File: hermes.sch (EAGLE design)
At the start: 36 parts, among them IC1 MIC5219-3.3BML

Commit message: -Update Library -Correct P2P pins -Place general position of components
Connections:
- net +3V3: now also IC1G$1.OUT; no longer IC1.OUT
- net GND: now also CONN2-3.P$1, IC1-DICE.P$1, IC1G$1.GND; no longer CONN2-2.P$1, IC1.GND
- net N$2: now also IC1G$1.PG; no longer IC1.PG
- net SERCOM5_SCL: now also CONN2-1.P$1; no longer CONN2-4.P$1
- net SERCOM5_SDA: now also CONN2-2.P$1; no longer CONN2-3.P$1
- net VCC: now also CONN2-4.P$1, IC1G$1.EN, IC1G$1.IN; no longer CONN2-1.P$1, IC1.EN, IC1.IN
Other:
- moved on the sheet: CONN2-1, CONN2-2, CONN2-3, CONN2-4
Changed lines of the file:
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@@
 <instance part="CONN1" gate="-3" x="119.38" y="40.64" rot="MR0"/>
 <instance part="CONN1" gate="-4" x="119.38" y="35.56" rot="MR0"/>
-<instance part="CONN2" gate="-1" x="127" y="60.96"/>
-<instance part="CONN2" gate="-2" x="127" y="55.88"/>
-<instance part="CONN2" gate="-3" x="127" y="40.64"/>
-<instance part="CONN2" gate="-4" x="127" y="35.56"/>
+<instance part="CONN2" gate="-1" x="127" y="35.56" rot="MR180"/>
+<instance part="CONN2" gate="-3" x="127" y="55.88"/>
+<instance part="CONN2" gate="-2" x="127" y="40.64"/>
+<instance part="CONN2" gate="-4" x="127" y="60.96"/>
 <instance part="U$1" gate="-1" x="20.32" y="60.96" rot="MR0"/>
 <instance part="U$1" gate="-2" x="20.32" y="55.88" rot="MR0"/>
@@
 <instance part="U$1" gate="-DICE" x="185.42" y="50.8" rot="R180"/>
 <instance part="GND14" gate="1" x="187.96" y="45.72"/>
+<instance part="IC1" gate="-DICE" x="185.42" y="66.04" rot="R180"/>
 </instances>
 <busses>
@@
 <junction x="124.46" y="55.88"/>
 <pinref part="CONN1" gate="-2" pin="P$1"/>
-<pinref part="CONN2" gate="-2" pin="P$1"/>
+<pinref part="CONN2" gate="-3" pin="P$1"/>
 </segment>
 <segment>
@@
 <wire x1="185.42" y1="50.8" x2="187.96" y2="50.8" width="0.1524" layer="91"/>
 <junction x="187.96" y="50.8"/>
+<pinref part="IC1" gate="-DICE" pin="P$1"/>
+<wire x1="185.42" y1="66.04" x2="187.96" y2="66.04" width="0.1524" layer="91"/>
+<wire x1="187.96" y1="66.04" x2="187.96" y2="60.96" width="0.1524" layer="91"/>
+<junction x="187.96" y="60.96"/>
 </segment>
 </net>
@@
 <wire x1="119.38" y1="60.96" x2="124.46" y2="60.96" width="0.1524" layer="91"/>
 <pinref part="P+3" gate="VCC" pin="VCC"/>
-<wire x1="124.46" y1="60.96" x2="127" y2="60.96" width="0.1524" layer="91"/>
 <wire x1="124.46" y1="63.5" x2="124.46" y2="60.96" width="0.1524" layer="91"/>
+<pinref part="CONN1" gate="-1" pin="P$1"/>
+<pinref part="CONN2" gate="-4" pin="P$1"/>
+<wire x1="127" y1="60.96" x2="124.46" y2="60.96" width="0.1524" layer="91"/>
 <junction x="124.46" y="60.96"/>
-<pinref part="CONN1" gate="-1" pin="P$1"/>
-<pinref part="CONN2" gate="-1" pin="P$1"/>
 </segment>
 </net>
@@
 <label x="127" y="33.02" size="1.27" layer="95" xref="yes"/>
 <pinref part="CONN1" gate="-3" pin="P$1"/>
-<pinref part="CONN2" gate="-3" pin="P$1"/>
+<pinref part="CONN2" gate="-2" pin="P$1"/>
 </segment>
 </net>
@@
 <net name="SERCOM5_SCL" class="0">
 <segment>
-<wire x1="127" y1="35.56" x2="121.92" y2="35.56" width="0.1524" layer="91"/>
 <wire x1="121.92" y1="35.56" x2="119.38" y2="35.56" width="0.1524" layer="91"/>
 <wire x1="121.92" y1="35.56" x2="121.92" y2="30.48" width="0.1524" layer="91"/>
-<junction x="121.92" y="35.56"/>
 <wire x1="121.92" y1="30.48" x2="127" y2="30.48" width="0.1524" layer="91"/>
 <label x="127" y="30.48" size="1.27" layer="95" xref="yes"/>
 <pinref part="CONN1" gate="-4" pin="P$1"/>
-<pinref part="CONN2" gate="-4" pin="P$1"/>
-</segment>
-</net>
+<pinref part="CONN2" gate="-1" pin="P$1"/>
+<wire x1="127" y1="35.56" x2="121.92" y2="35.56" width="0.1524" layer="91"/>
+<junction x="121.92" y="35.56"/>
+</segment>
+</net>

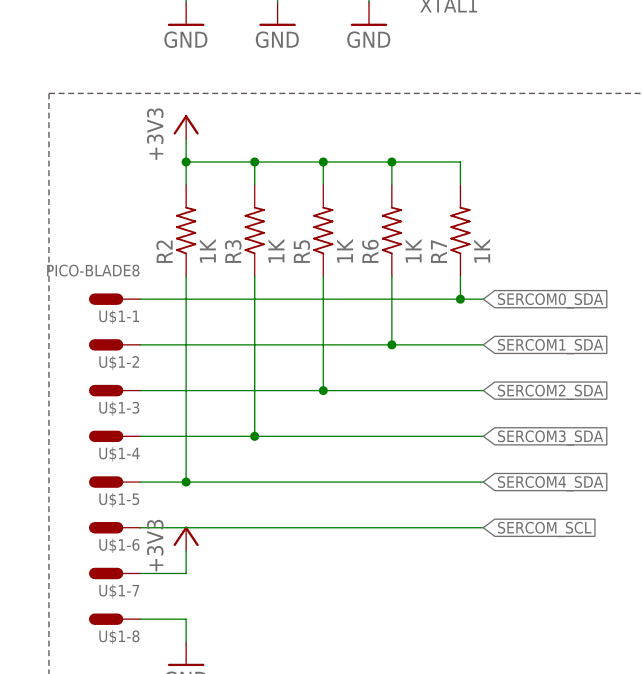
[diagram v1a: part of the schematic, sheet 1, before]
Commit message: MIniaturization of board process
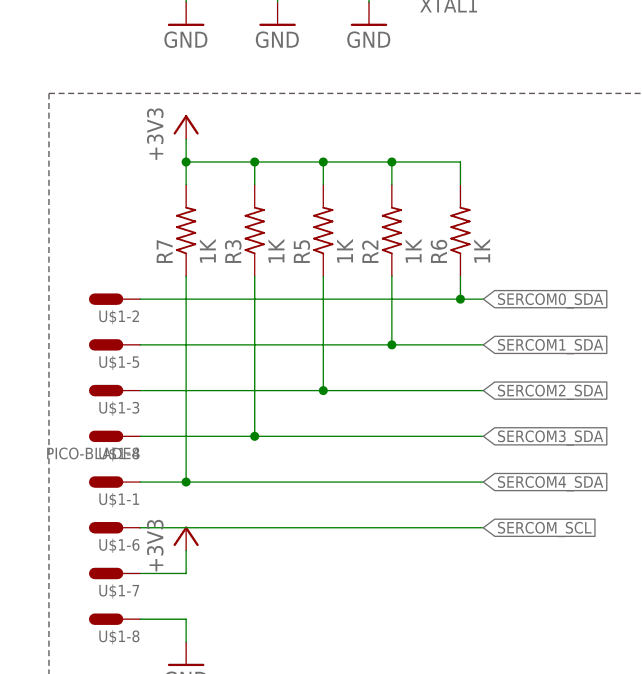
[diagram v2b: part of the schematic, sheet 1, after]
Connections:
- net SERCOM0_SDA: now also R6.1, U$1-2.P$1; no longer R7.1, U$1-1.P$1
- net SERCOM1_SDA: now also R2.1, U$1-5.P$1; no longer R6.1, U$1-2.P$1
- net SERCOM4_SDA: now also R7.1, U$1-1.P$1; no longer R2.1, U$1-5.P$1
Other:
- moved on the sheet: R2, R6, R7, U$1-1, U$1-2, U$1-5
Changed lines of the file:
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@@
 <instance part="GND5" gate="1" x="45.72" y="104.14"/>
 <instance part="+3V31" gate="G$1" x="25.4" y="81.28"/>
-<instance part="R7" gate="G$1" x="55.88" y="68.58" rot="R90"/>
-<instance part="R6" gate="G$1" x="48.26" y="68.58" rot="R90"/>
+<instance part="R7" gate="G$1" x="25.4" y="68.58" rot="R90"/>
+<instance part="R6" gate="G$1" x="55.88" y="68.58" rot="R90"/>
 <instance part="R5" gate="G$1" x="40.64" y="68.58" rot="R90"/>
 <instance part="R3" gate="G$1" x="33.02" y="68.58" rot="R90"/>
-<instance part="R2" gate="G$1" x="25.4" y="68.58" rot="R90"/>
+<instance part="R2" gate="G$1" x="48.26" y="68.58" rot="R90"/>
 <instance part="FRAME1" gate="G$1" x="0" y="0"/>
 <instance part="C1" gate="G$1" x="50.8" y="139.7"/>
@@
 <instance part="CONN2" gate="-2" x="127" y="40.64"/>
 <instance part="CONN2" gate="-4" x="127" y="60.96"/>
-<instance part="U$1" gate="-1" x="20.32" y="60.96" rot="MR0"/>
-<instance part="U$1" gate="-2" x="20.32" y="55.88" rot="MR0"/>
+<instance part="U$1" gate="-1" x="20.32" y="40.64" rot="MR0"/>
+<instance part="U$1" gate="-5" x="20.32" y="55.88" rot="MR0"/>
 <instance part="U$1" gate="-3" x="20.32" y="50.8" rot="MR0"/>
 <instance part="U$1" gate="-4" x="20.32" y="45.72" rot="MR0"/>
-<instance part="U$1" gate="-5" x="20.32" y="40.64" rot="MR0"/>
+<instance part="U$1" gate="-2" x="20.32" y="60.96" rot="MR0"/>
 <instance part="U$1" gate="-6" x="20.32" y="35.56" rot="MR0"/>
 <instance part="U$1" gate="-7" x="20.32" y="30.48" rot="MR0"/>
@@
 </segment>
 <segment>
-<pinref part="R2" gate="G$1" pin="2"/>
 <wire x1="55.88" y1="76.2" x2="48.26" y2="76.2" width="0.1524" layer="91"/>
 <wire x1="48.26" y1="76.2" x2="40.64" y2="76.2" width="0.1524" layer="91"/>
 <wire x1="40.64" y1="76.2" x2="33.02" y2="76.2" width="0.1524" layer="91"/>
 <wire x1="33.02" y1="76.2" x2="25.4" y2="76.2" width="0.1524" layer="91"/>
-<wire x1="25.4" y1="76.2" x2="25.4" y2="73.66" width="0.1524" layer="91"/>
 <pinref part="R3" gate="G$1" pin="2"/>
 <wire x1="33.02" y1="73.66" x2="33.02" y2="76.2" width="0.1524" layer="91"/>
@@
 <wire x1="40.64" y1="73.66" x2="40.64" y2="76.2" width="0.1524" layer="91"/>
 <junction x="40.64" y="76.2"/>
-<pinref part="R6" gate="G$1" pin="2"/>
+<pinref part="+3V31" gate="G$1" pin="+3V3"/>
+<wire x1="25.4" y1="78.74" x2="25.4" y2="76.2" width="0.1524" layer="91"/>
+<pinref part="R7" gate="G$1" pin="2"/>
+<wire x1="25.4" y1="73.66" x2="25.4" y2="76.2" width="0.1524" layer="91"/>
+<junction x="25.4" y="76.2"/>
+<pinref part="R2" gate="G$1" pin="2"/>
 <wire x1="48.26" y1="73.66" x2="48.26" y2="76.2" width="0.1524" layer="91"/>
 <junction x="48.26" y="76.2"/>
-<pinref part="R7" gate="G$1" pin="2"/>
+<pinref part="R6" gate="G$1" pin="2"/>
 <wire x1="55.88" y1="73.66" x2="55.88" y2="76.2" width="0.1524" layer="91"/>
-<pinref part="+3V31" gate="G$1" pin="+3V3"/>
-<wire x1="25.4" y1="78.74" x2="25.4" y2="76.2" width="0.1524" layer="91"/>
-<junction x="25.4" y="76.2"/>
 </segment>
 <segment>
@@
 <net name="SERCOM0_SDA" class="0">
 <segment>
-<pinref part="R7" gate="G$1" pin="1"/>
+<label x="58.42" y="60.96" size="1.27" layer="95" xref="yes"/>
+<pinref part="R6" gate="G$1" pin="1"/>
+<wire x1="55.88" y1="60.96" x2="58.42" y2="60.96" width="0.1524" layer="91"/>
 <wire x1="55.88" y1="63.5" x2="55.88" y2="60.96" width="0.1524" layer="91"/>
-<wire x1="55.88" y1="60.96" x2="58.42" y2="60.96" width="0.1524" layer="91"/>
-<label x="58.42" y="60.96" size="1.27" layer="95" xref="yes"/>
+<pinref part="U$1" gate="-2" pin="P$1"/>
 <wire x1="20.32" y1="60.96" x2="55.88" y2="60.96" width="0.1524" layer="91"/>
 <junction x="55.88" y="60.96"/>
-<pinref part="U$1" gate="-1" pin="P$1"/>
 </segment>
 </net>
 <net name="SERCOM1_SDA" class="0">
 <segment>
-<pinref part="R6" gate="G$1" pin="1"/>
-<wire x1="48.26" y1="63.5" x2="48.26" y2="55.88" width="0.1524" layer="91"/>
-<wire x1="48.26" y1="55.88" x2="58.42" y2="55.88" width="0.1524" layer="91"/>
 <label x="58.42" y="55.88" size="1.27" layer="95" xref="yes"/>
 <wire x1="20.32" y1="55.88" x2="48.26" y2="55.88" width="0.1524" layer="91"/>
+<pinref part="U$1" gate="-5" pin="P$1"/>
+<pinref part="R2" gate="G$1" pin="1"/>
+<wire x1="48.26" y1="55.88" x2="58.42" y2="55.88" width="0.1524" layer="91"/>
+<wire x1="48.26" y1="63.5" x2="48.26" y2="55.88" width="0.1524" layer="91"/>
 <junction x="48.26" y="55.88"/>
-<pinref part="U$1" gate="-2" pin="P$1"/>
 </segment>
 </net>
@@
 <net name="SERCOM4_SDA" class="0">
 <segment>
-<pinref part="R2" gate="G$1" pin="1"/>
+<label x="58.42" y="40.64" size="1.27" layer="95" xref="yes"/>
+<pinref part="R7" gate="G$1" pin="1"/>
+<wire x1="25.4" y1="40.64" x2="58.42" y2="40.64" width="0.1524" layer="91"/>
 <wire x1="25.4" y1="63.5" x2="25.4" y2="40.64" width="0.1524" layer="91"/>
-<wire x1="25.4" y1="40.64" x2="58.42" y2="40.64" width="0.1524" layer="91"/>
-<label x="58.42" y="40.64" size="1.27" layer="95" xref="yes"/>
+<pinref part="U$1" gate="-1" pin="P$1"/>
 <wire x1="20.32" y1="40.64" x2="25.4" y2="40.64" width="0.1524" layer="91"/>
 <junction x="25.4" y="40.64"/>
-<pinref part="U$1" gate="-5" pin="P$1"/>
-</segment>
-</net>
+</segment>
+</net>

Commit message: First release of Hermes, Add Layout view and CAM files, Correct minor issues
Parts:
- renumbered CONN1 to PEER1, CONN2 to PEER2, IC1 to VDO, PIN10 to PIN2, PIN11 to PIN3, PIN12 to PIN4, PIN13 to PIN5, PIN14 to PIN6, PIN9 to PIN1, TP1 to VCC, TP2 to 3V3, TP3 to GND, U$1 to SLAVE, XTAL1 to XTAL
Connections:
- net SERCOM0_SDA: now also R7.1; no longer R6.1
- net SERCOM1_SDA: now also R6.1; no longer R2.1
- net SERCOM4_SDA: now also R2.1; no longer R7.1

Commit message: Replace components according to availability in digital stores (Capacitors and Inductors)
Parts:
- removed L1: 10uH, rcl:L-USL0201
- added L2: 10uH, Hermes_lib:SPM5030-HZ
- C5, C6: device rcl:C-USC0201 -> rcl:C-USC0402
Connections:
- net +3V3: now also L2.P$2; no longer L1.1
- net N$1: now also L2.P$1; no longer L1.2
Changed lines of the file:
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@@
 <part name="+3V35" library="supply1" library_urn="urn:adsk.eagle:library:371" deviceset="+3V3" device=""/>
 <part name="GND10" library="supply1" library_urn="urn:adsk.eagle:library:371" deviceset="GND" device=""/>
-<part name="L1" library="rcl" library_urn="urn:adsk.eagle:library:334" deviceset="L-US" device="L0201" package3d_urn="urn:adsk.eagle:package:23513/1" value="10uH"/>
 <part name="C7" library="rcl" library_urn="urn:adsk.eagle:library:334" deviceset="C-US" device="C0201" package3d_urn="urn:adsk.eagle:package:23690/1" value="100nF"/>
-<part name="C6" library="rcl" library_urn="urn:adsk.eagle:library:334" deviceset="C-US" device="C0201" package3d_urn="urn:adsk.eagle:package:23690/1" value="10uF"/>
-<part name="C5" library="rcl" library_urn="urn:adsk.eagle:library:334" deviceset="C-US" device="C0201" package3d_urn="urn:adsk.eagle:package:23690/1" value="10uF"/>
+<part name="C6" library="rcl" library_urn="urn:adsk.eagle:library:334" deviceset="C-US" device="C0402" package3d_urn="urn:adsk.eagle:package:23626/1" value="10uF"/>
+<part name="C5" library="rcl" library_urn="urn:adsk.eagle:library:334" deviceset="C-US" device="C0402" package3d_urn="urn:adsk.eagle:package:23626/1" value="10uF"/>
 <part name="C10" library="rcl" library_urn="urn:adsk.eagle:library:334" deviceset="C-US" device="C0201" package3d_urn="urn:adsk.eagle:package:23690/1" value="100nF"/>
 <part name="C8" library="rcl" library_urn="urn:adsk.eagle:library:334" deviceset="C-US" device="C0201" package3d_urn="urn:adsk.eagle:package:23690/1" value="100nF"/>
@@
 <part name="SLAVE" library="Hermes_lib" deviceset="PICO-BLADE8" device=""/>
 <part name="GND14" library="supply1" library_urn="urn:adsk.eagle:library:371" deviceset="GND" device=""/>
+<part name="L2" library="Hermes_lib" deviceset="SPM5030-HZ" device="" value="10uH"/>
 </parts>
 <sheets>
@@
 <instance part="+3V35" gate="G$1" x="96.52" y="160.02"/>
 <instance part="GND10" gate="1" x="106.68" y="106.68"/>
-<instance part="L1" gate="G$1" x="106.68" y="142.24"/>
 <instance part="C7" gate="G$1" x="119.38" y="124.46"/>
 <instance part="C6" gate="G$1" x="106.68" y="124.46"/>
@@
 <instance part="GND14" gate="1" x="187.96" y="45.72"/>
 <instance part="VDO" gate="-DICE" x="185.42" y="66.04" rot="R180"/>
+<instance part="L2" gate="G$1" x="106.68" y="142.24" rot="MR90"/>
 </instances>
 <busses>
@@
 <segment>
 <pinref part="UC1" gate="_PWR" pin="VDDANA"/>
-<pinref part="L1" gate="G$1" pin="2"/>
 <wire x1="129.54" y1="132.08" x2="119.38" y2="132.08" width="0.1524" layer="91"/>
 <pinref part="C6" gate="G$1" pin="1"/>
 <wire x1="119.38" y1="132.08" x2="106.68" y2="132.08" width="0.1524" layer="91"/>
-<wire x1="106.68" y1="132.08" x2="106.68" y2="134.62" width="0.1524" layer="91"/>
 <wire x1="106.68" y1="127" x2="106.68" y2="132.08" width="0.1524" layer="91"/>
 <junction x="106.68" y="132.08"/>
@@
 <wire x1="119.38" y1="127" x2="119.38" y2="132.08" width="0.1524" layer="91"/>
 <junction x="119.38" y="132.08"/>
+<pinref part="L2" gate="G$1" pin="P$1"/>
+<wire x1="106.68" y1="132.08" x2="106.68" y2="137.16" width="0.1524" layer="91"/>
 </segment>
 </net>
@@
 <junction x="96.52" y="152.4"/>
 <wire x1="106.68" y1="152.4" x2="96.52" y2="152.4" width="0.1524" layer="91"/>
-<pinref part="L1" gate="G$1" pin="1"/>
-<wire x1="106.68" y1="149.86" x2="106.68" y2="152.4" width="0.1524" layer="91"/>
 <junction x="106.68" y="152.4"/>
+<pinref part="L2" gate="G$1" pin="P$2"/>
+<wire x1="106.68" y1="147.32" x2="106.68" y2="152.4" width="0.1524" layer="91"/>
 </segment>
 <segment>

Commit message: -Update component description in library -Generate new BOM and CAM files from new configuration -Delete outdated layout and cam documents
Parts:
- removed C1: 470pF, rcl:C-USC0201
- removed VDO: MIC5219-3.3BML, Hermes_lib:MIC5219-3.3BML
- added LDO1: MIC5231-3.3BM5, Hermes_lib:MIC5231-3.3BM5
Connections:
- removed net N$2: C1.1, VDOG$1.PG
- net +3V3: now also LDO1.OUT; no longer VDOG$1.OUT
- net GND: now also LDO1.GND; no longer C1.2, VDO-DICE.P$1, VDOG$1.GND
- net VCC: now also LDO1.EN, LDO1.IN; no longer VDOG$1.EN, VDOG$1.IN
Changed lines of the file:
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@@
 <part name="C11" library="rcl" library_urn="urn:adsk.eagle:library:334" deviceset="C-US" device="C0201" package3d_urn="urn:adsk.eagle:package:23690/1" value="1uF"/>
 <part name="C9" library="rcl" library_urn="urn:adsk.eagle:library:334" deviceset="C-US" device="C0201" package3d_urn="urn:adsk.eagle:package:23690/1" value="100nF"/>
-<part name="VDO" library="Hermes_lib" deviceset="MIC5219-" device="3.3BML"/>
 <part name="C4" library="rcl" library_urn="urn:adsk.eagle:library:334" deviceset="C-US" device="C0201" package3d_urn="urn:adsk.eagle:package:23690/1" value="2.2uF"/>
 <part name="P+1" library="supply1" library_urn="urn:adsk.eagle:library:371" deviceset="VCC" device=""/>
@@
 <part name="FRAME2" library="frames" library_urn="urn:adsk.eagle:library:229" deviceset="A4L-LOC" device=""/>
 <part name="FRAME1" library="frames" library_urn="urn:adsk.eagle:library:229" deviceset="A4L-LOC" device=""/>
-<part name="C1" library="rcl" library_urn="urn:adsk.eagle:library:334" deviceset="C-US" device="C0201" package3d_urn="urn:adsk.eagle:package:23690/1" value="470pF"/>
-<part name="GND7" library="supply1" library_urn="urn:adsk.eagle:library:371" deviceset="GND" device=""/>
 <part name="XTAL" library="Hermes_lib" deviceset="LFXTAL059596CUTT" device=""/>
 <part name="GND6" library="supply1" library_urn="urn:adsk.eagle:library:371" deviceset="GND" device=""/>
@@
 <part name="GND14" library="supply1" library_urn="urn:adsk.eagle:library:371" deviceset="GND" device=""/>
 <part name="L2" library="Hermes_lib" deviceset="SPM5030-HZ" device="" value="10uH"/>
+<part name="LDO1" library="Hermes_lib" deviceset="MIC5231-" device="3.3BM5"/>
 </parts>
 <sheets>
@@
 <instance part="C11" gate="G$1" x="172.72" y="139.7" rot="R90"/>
 <instance part="C9" gate="G$1" x="121.92" y="139.7" rot="R270"/>
-<instance part="VDO" gate="G$1" x="38.1" y="147.32"/>
 <instance part="C4" gate="G$1" x="58.42" y="139.7"/>
 <instance part="P+1" gate="VCC" x="25.4" y="160.02"/>
@@
 <instance part="R6" gate="G$1" x="48.26" y="68.58" rot="R90"/>
 <instance part="FRAME1" gate="G$1" x="0" y="0"/>
-<instance part="C1" gate="G$1" x="50.8" y="139.7"/>
-<instance part="GND7" gate="1" x="50.8" y="129.54"/>
 <instance part="XTAL" gate="G$1" x="53.34" y="97.79" rot="R180"/>
 <instance part="GND6" gate="1" x="45.72" y="91.44"/>
@@
 <instance part="SLAVE" gate="-DICE" x="185.42" y="50.8" rot="R180"/>
 <instance part="GND14" gate="1" x="187.96" y="45.72"/>
-<instance part="VDO" gate="-DICE" x="185.42" y="66.04" rot="R180"/>
 <instance part="L2" gate="G$1" x="106.68" y="142.24" rot="MR90"/>
+<instance part="LDO1" gate="G$1" x="38.1" y="147.32"/>
 </instances>
 <busses>
@@
 </segment>
 <segment>
-<pinref part="VDO" gate="G$1" pin="OUT"/>
 <pinref part="C4" gate="G$1" pin="1"/>
 <wire x1="48.26" y1="149.86" x2="58.42" y2="149.86" width="0.1524" layer="91"/>
@@
 <wire x1="58.42" y1="152.4" x2="58.42" y2="149.86" width="0.1524" layer="91"/>
 <junction x="58.42" y="149.86"/>
+<pinref part="LDO1" gate="G$1" pin="OUT"/>
 </segment>
 <segment>
@@
 <segment>
 <pinref part="GND1" gate="1" pin="GND"/>
-<pinref part="VDO" gate="G$1" pin="GND"/>
 <wire x1="25.4" y1="142.24" x2="25.4" y2="139.7" width="0.1524" layer="91"/>
 <wire x1="27.94" y1="142.24" x2="25.4" y2="142.24" width="0.1524" layer="91"/>
+<pinref part="LDO1" gate="G$1" pin="GND"/>
 </segment>
 <segment>
@@
 <wire x1="45.72" y1="106.68" x2="45.72" y2="109.22" width="0.1524" layer="91"/>
 <junction x="45.72" y="109.22"/>
-</segment>
-<segment>
-<pinref part="C1" gate="G$1" pin="2"/>
-<pinref part="GND7" gate="1" pin="GND"/>
-<wire x1="50.8" y1="134.62" x2="50.8" y2="132.08" width="0.1524" layer="91"/>
 </segment>
 <segment>
@@
 <wire x1="185.42" y1="50.8" x2="187.96" y2="50.8" width="0.1524" layer="91"/>
 <junction x="187.96" y="50.8"/>
-<pinref part="VDO" gate="-DICE" pin="P$1"/>
-<wire x1="185.42" y1="66.04" x2="187.96" y2="66.04" width="0.1524" layer="91"/>
-<wire x1="187.96" y1="66.04" x2="187.96" y2="60.96" width="0.1524" layer="91"/>
-<junction x="187.96" y="60.96"/>
 </segment>
 </net>
@@
 <segment>
 <pinref part="P+1" gate="VCC" pin="VCC"/>
-<pinref part="VDO" gate="G$1" pin="IN"/>
 <wire x1="27.94" y1="152.4" x2="25.4" y2="152.4" width="0.1524" layer="91"/>
 <wire x1="25.4" y1="152.4" x2="25.4" y2="157.48" width="0.1524" layer="91"/>
@@
 <wire x1="25.4" y1="147.32" x2="27.94" y2="147.32" width="0.1524" layer="91"/>
 <junction x="25.4" y="152.4"/>
-<pinref part="VDO" gate="G$1" pin="EN"/>
+<pinref part="LDO1" gate="G$1" pin="IN"/>
+<pinref part="LDO1" gate="G$1" pin="EN"/>
 </segment>
 <segment>
@@
 </segment>
 </net>
-<net name="N$2" class="0">
-<segment>
-<pinref part="VDO" gate="G$1" pin="PG"/>
-<pinref part="C1" gate="G$1" pin="1"/>
-<wire x1="48.26" y1="144.78" x2="50.8" y2="144.78" width="0.1524" layer="91"/>
-<wire x1="50.8" y1="144.78" x2="50.8" y2="142.24" width="0.1524" layer="91"/>
-</segment>
-</net>
